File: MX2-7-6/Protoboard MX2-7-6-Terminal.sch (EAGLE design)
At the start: 293 parts

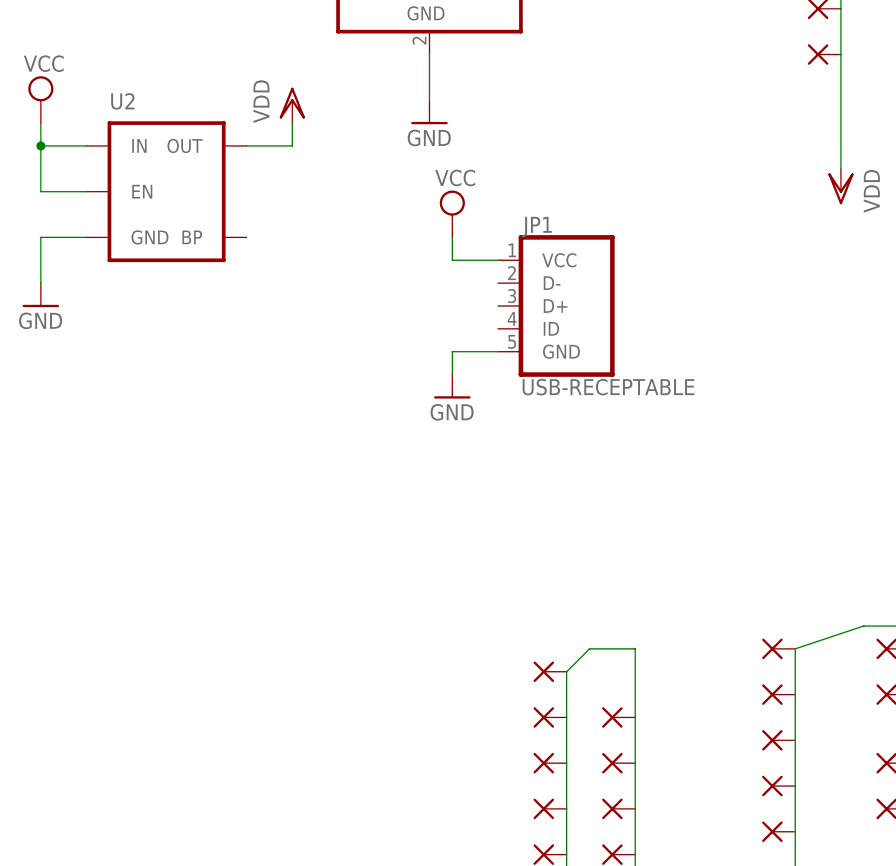
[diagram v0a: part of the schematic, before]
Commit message: Change usb connector
Change to correct usb connecter and moved esp8266 bit more onto the
board.
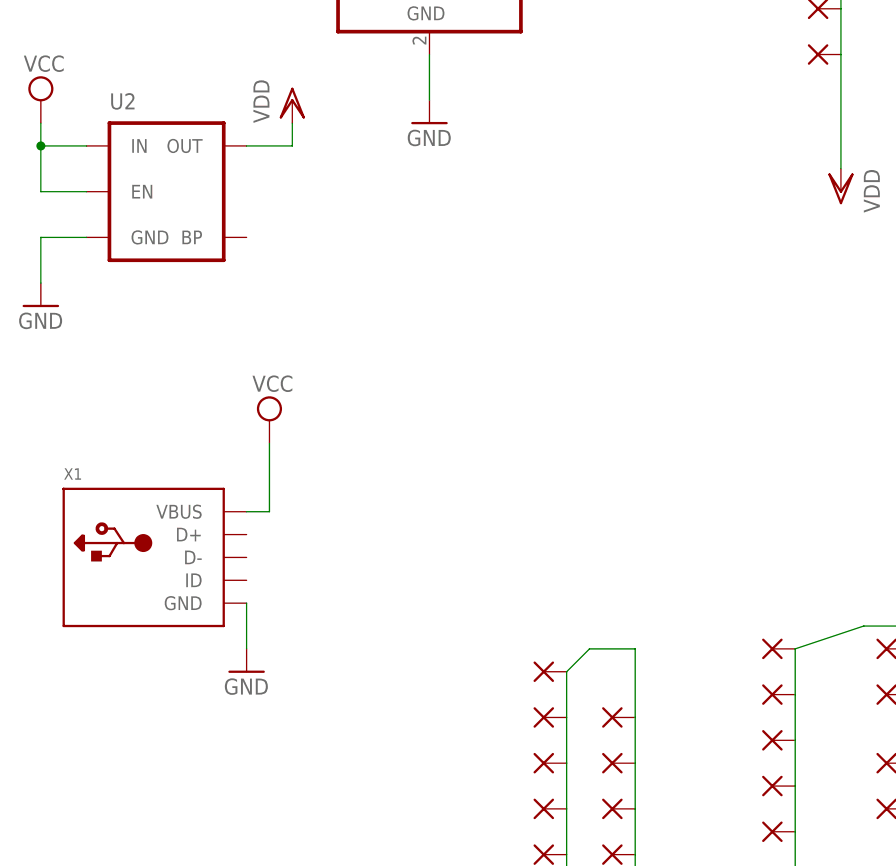
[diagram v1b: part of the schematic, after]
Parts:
- removed JP1: USB-RECEPTABLE, daspilker:USB-RECEPTABLE
- added X1: (no value), microbuilder:USBMICRO_20329
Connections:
- net GND: now also X1.GND; no longer JP1.GND
- net VCC: now also X1.VBUS; no longer JP1.VCC
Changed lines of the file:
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@@
 <part name="PAD38" library="wirepad" deviceset="1,6/0,8" device=""/>
 <part name="GND1" library="supply1" deviceset="GND" device=""/>
-<part name="JP1" library="daspilker" deviceset="USB-RECEPTABLE" device=""/>
-<part name="SUPPLY1" library="supply2" deviceset="VCC" device=""/>
-<part name="GND3" library="supply1" deviceset="GND" device=""/>
 <part name="SUPPLY2" library="supply2" deviceset="VCC" device=""/>
 <part name="GND5" library="supply1" deviceset="GND" device=""/>
@@
 <part name="JP7" library="adafruit" deviceset="PINHD-1X1" device="CB"/>
 <part name="JP8" library="adafruit" deviceset="PINHD-1X1" device="CB"/>
+<part name="X1" library="microbuilder" deviceset="USB" device="MICRO_20329"/>
+<part name="SUPPLY3" library="supply2" deviceset="VCC" device=""/>
+<part name="GND6" library="supply1" deviceset="GND" device=""/>
 </parts>
 <sheets>
@@
 </instance>
 <instance part="GND1" gate="1" x="38.1" y="40.64"/>
-<instance part="JP1" gate="G$1" x="-12.7" y="27.94"/>
-<instance part="SUPPLY1" gate="G$1" x="-25.4" y="38.1"/>
-<instance part="GND3" gate="1" x="-25.4" y="17.78"/>
 <instance part="SUPPLY2" gate="G$1" x="-71.12" y="50.8"/>
 <instance part="GND5" gate="1" x="-71.12" y="27.94"/>
@@
 <instance part="JP7" gate="G$1" x="170.18" y="-35.56" rot="R180"/>
 <instance part="JP8" gate="G$1" x="170.18" y="-40.64" rot="R180"/>
+<instance part="X1" gate="G$1" x="-58.42" y="0"/>
+<instance part="SUPPLY3" gate="G$1" x="-45.72" y="15.24"/>
+<instance part="GND6" gate="1" x="-48.26" y="-12.7"/>
 </instances>
 <busses>
@@
 </segment>
 <segment>
-<pinref part="JP1" gate="G$1" pin="GND"/>
-<pinref part="GND3" gate="1" pin="GND"/>
-<wire x1="-20.32" y1="22.86" x2="-25.4" y2="22.86" width="0.1524" layer="91"/>
-<wire x1="-25.4" y1="22.86" x2="-25.4" y2="20.32" width="0.1524" layer="91"/>
-</segment>
-<segment>
 <pinref part="GND5" gate="1" pin="GND"/>
 <wire x1="-71.12" y1="30.48" x2="-71.12" y2="35.56" width="0.1524" layer="91"/>
@@
 <wire x1="-71.12" y1="35.56" x2="-66.04" y2="35.56" width="0.1524" layer="91"/>
 </segment>
+<segment>
+<pinref part="X1" gate="G$1" pin="GND"/>
+<pinref part="GND6" gate="1" pin="GND"/>
+<wire x1="-48.26" y1="-5.08" x2="-48.26" y2="-10.16" width="0.1524" layer="91"/>
+</segment>
 </net>
 <net name="VCC" class="0">
@@
 <pinref part="DC" gate="G$1" pin="VIN"/>
 <wire x1="-45.72" y1="63.5" x2="-40.64" y2="63.5" width="0.1524" layer="91"/>
-</segment>
-<segment>
-<pinref part="JP1" gate="G$1" pin="VCC"/>
-<pinref part="SUPPLY1" gate="G$1" pin="VCC"/>
-<wire x1="-20.32" y1="33.02" x2="-25.4" y2="33.02" width="0.1524" layer="91"/>
-<wire x1="-25.4" y1="33.02" x2="-25.4" y2="35.56" width="0.1524" layer="91"/>
 </segment>
 <segment>
@@
 <junction x="-71.12" y="45.72"/>
 </segment>
-</net>
+<segment>
+<pinref part="X1" gate="G$1" pin="VBUS"/>
+<pinref part="SUPPLY3" gate="G$1" pin="VCC"/>
+<wire x1="-48.26" y1="5.08" x2="-45.72" y2="5.08" width="0.1524" layer="91"/>
+<wire x1="-45.72" y1="5.08" x2="-45.72" y2="12.7" width="0.1524" layer="91"/>
+</segment>
+</net>

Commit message: Update esp component and usb
test
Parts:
- removed JP4: (no value), adafruit:PINHD-1X1-BIGPOGO
- removed JP6, JP7, JP8: (no value), adafruit:PINHD-1X1CB
- removed PAD1, PAD100, PAD101, PAD102, PAD103, PAD106, PAD107, PAD108, PAD109, PAD110, PAD111, PAD112, PAD115, PAD116, PAD117, PAD118, PAD119, PAD120, PAD121, PAD124, PAD125, PAD126, PAD127, PAD128, PAD129, PAD130, PAD133, PAD134, PAD135, PAD136, PAD137, PAD138, PAD139, PAD142, PAD143, PAD144, PAD145, PAD146, PAD147, PAD148, PAD151, PAD152, PAD153, PAD154, PAD155, PAD156, PAD157, PAD160, PAD161, PAD162, PAD163, PAD164, PAD165, PAD166, PAD169, PAD170, PAD171, PAD172, PAD173, PAD174, PAD175, PAD178, PAD179, PAD180, PAD181, PAD182, PAD183, PAD184, PAD187, PAD188, PAD189, PAD190, PAD191, PAD192, PAD193, PAD196, PAD197, PAD198, PAD199, PAD2, PAD200, PAD201, PAD202, PAD205, PAD206, PAD207, PAD208, PAD209, PAD210, PAD211, PAD214, PAD215, PAD216, PAD217, PAD218, PAD219, PAD220, PAD260, PAD261, PAD262, PAD263, PAD264, PAD265, PAD266, PAD269, PAD270, PAD271, PAD272, PAD273, PAD274, PAD275, PAD278, PAD279, PAD280, PAD281, PAD282, PAD283, PAD284, PAD287, PAD288, PAD289, PAD290, PAD291, PAD292, PAD293, PAD296, PAD297, PAD298, PAD299, PAD300, PAD301, PAD302, PAD305, PAD306, PAD307, PAD308, PAD309, PAD310, PAD311, PAD314, PAD315, PAD316, PAD317, PAD318, PAD319, PAD320, PAD332, PAD333, PAD334, PAD335, PAD336, PAD337, PAD338, PAD341, PAD342, PAD343, PAD344, PAD345, PAD346, PAD347, PAD350, PAD351, PAD352, PAD353, PAD354, PAD355, PAD356, PAD359, PAD360, PAD361, PAD362, PAD363, PAD364, PAD365, PAD368, PAD369, PAD370, PAD371, PAD372, PAD373, PAD374, PAD377, PAD378, PAD379, PAD380, PAD381, PAD382, PAD383, PAD385, PAD386, PAD387, PAD388, PAD389, PAD391, PAD392, PAD393, PAD394, PAD79, PAD80, PAD81, PAD82, PAD83, PAD84, PAD85, PAD88, PAD89, PAD90, PAD91, PAD92, PAD93, PAD94, PAD97, PAD98, PAD99: (no value), wirepad:1,6/0,8
- added J10, J11, J12, J13, J14, J15, J16, J17, J18, J19, J2, J20, J21, J22, J23, J24, J25, J26, J27, J28, J29, J3, J30, J4, J5, J6, J7, J8, J9: (no value), SparkFun-Connectors:M07NO_SILK
- added J31: (no value), SparkFun-Connectors:M05NO_SILK
- added J32: (no value), SparkFun-Connectors:M031X03_NO_SILK
- added J36, J37, J38: (no value), SparkFun-Connectors:M01PTH_NO_SILK_YES_STOP
- added JP1: (no value), adafruit:PINHD-1X1-BIGPOGO
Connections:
- removed net N$40: PAD377.P, PAD378.P, PAD379.P, PAD380.P, PAD381.P, PAD382.P, PAD383.P
- removed net N$41: PAD385.P, PAD386.P, PAD387.P, PAD388.P, PAD389.P
- new net N$6: J4.1, J4.2, J4.3, J4.4, J4.5, J4.6, J4.7
- net N$1: now also J2.1, J2.2, J2.3, J2.4, J2.5, J2.6, J2.7; no longer PAD391.P, PAD392.P, PAD393.P, PAD394.P
- net N$10: now also J8.1, J8.2, J8.3, J8.4, J8.5, J8.6, J8.7; no longer PAD106.P, PAD107.P, PAD108.P, PAD109.P, PAD110.P, PAD111.P, PAD112.P
- net N$11: now also J9.1, J9.2, J9.3, J9.4, J9.5, J9.6, J9.7; no longer PAD115.P, PAD116.P, PAD117.P, PAD118.P, PAD119.P, PAD120.P, PAD121.P
- net N$12: now also J10.1, J10.2, J10.3, J10.4, J10.5, J10.6, J10.7; no longer PAD124.P, PAD125.P, PAD126.P, PAD127.P, PAD128.P, PAD129.P, PAD130.P
- net N$13: now also J11.1, J11.2, J11.3, J11.4, J11.5, J11.6, J11.7; no longer PAD133.P, PAD134.P, PAD135.P, PAD136.P, PAD137.P, PAD138.P, PAD139.P
- net N$14: now also J12.1, J12.2, J12.3, J12.4, J12.5, J12.6, J12.7; no longer PAD142.P, PAD143.P, PAD144.P, PAD145.P, PAD146.P, PAD147.P, PAD148.P
- net N$15: now also J13.1, J13.2, J13.3, J13.4, J13.5, J13.6, J13.7; no longer PAD151.P, PAD152.P, PAD153.P, PAD154.P, PAD155.P, PAD156.P, PAD157.P
- net N$16: now also J14.1, J14.2, J14.3, J14.4, J14.5, J14.6, J14.7; no longer PAD160.P, PAD161.P, PAD162.P, PAD163.P, PAD164.P, PAD165.P, PAD166.P
- net N$17: now also J15.1, J15.2, J15.3, J15.4, J15.5, J15.6, J15.7; no longer PAD169.P, PAD170.P, PAD171.P, PAD172.P, PAD173.P, PAD174.P, PAD175.P
- net N$18: now also J16.1, J16.2, J16.3, J16.4, J16.5, J16.6, J16.7; no longer PAD178.P, PAD179.P, PAD180.P, PAD181.P, PAD182.P, PAD183.P, PAD184.P
- net N$19: now also J17.1, J17.2, J17.3, J17.4, J17.5, J17.6, J17.7; no longer PAD187.P, PAD188.P, PAD189.P, PAD190.P, PAD191.P, PAD192.P, PAD193.P
- net N$2: now also J36.1, JP3.1; no longer JP2.1, JP6.1
- net N$20: now also J18.1, J18.2, J18.3, J18.4, J18.5, J18.6, J18.7; no longer PAD196.P, PAD197.P, PAD198.P, PAD199.P, PAD200.P, PAD201.P, PAD202.P
- net N$21: now also J19.1, J19.2, J19.3, J19.4, J19.5, J19.6, J19.7; no longer PAD205.P, PAD206.P, PAD207.P, PAD208.P, PAD209.P, PAD210.P, PAD211.P
- net N$22: now also J20.1, J20.2, J20.3, J20.4, J20.5, J20.6, J20.7; no longer PAD214.P, PAD215.P, PAD216.P, PAD217.P, PAD218.P, PAD219.P, PAD220.P
- net N$27: now also J21.1, J21.2, J21.3, J21.4, J21.5, J21.6, J21.7; no longer PAD260.P, PAD261.P, PAD262.P, PAD263.P, PAD264.P, PAD265.P, PAD266.P
- net N$28: now also J22.1, J22.2, J22.3, J22.4, J22.5, J22.6, J22.7; no longer PAD269.P, PAD270.P, PAD271.P, PAD272.P, PAD273.P, PAD274.P, PAD275.P
- net N$29: now also J23.1, J23.2, J23.3, J23.4, J23.5, J23.6, J23.7; no longer PAD278.P, PAD279.P, PAD280.P, PAD281.P, PAD282.P, PAD283.P, PAD284.P
- net N$3: now also J37.1, JP2.1; no longer PAD1.P, PAD2.P
- net N$30: now also J24.1, J24.2, J24.3, J24.4, J24.5, J24.6, J24.7; no longer PAD287.P, PAD288.P, PAD289.P, PAD290.P, PAD291.P, PAD292.P, PAD293.P
- net N$31: now also J25.1, J25.2, J25.3, J25.4, J25.5, J25.6, J25.7; no longer PAD296.P, PAD297.P, PAD298.P, PAD299.P, PAD300.P, PAD301.P, PAD302.P
- net N$32: now also J26.1, J26.2, J26.3, J26.4, J26.5, J26.6, J26.7; no longer PAD305.P, PAD306.P, PAD307.P, PAD308.P, PAD309.P, PAD310.P, PAD311.P
- net N$33: now also J27.1, J27.2, J27.3, J27.4, J27.5, J27.6, J27.7; no longer PAD314.P, PAD315.P, PAD316.P, PAD317.P, PAD318.P, PAD319.P, PAD320.P
- net N$35: now also J28.1, J28.2, J28.3, J28.4, J28.5, J28.6, J28.7; no longer PAD332.P, PAD333.P, PAD334.P, PAD335.P, PAD336.P, PAD337.P, PAD338.P
- net N$36: now also J29.1, J29.2, J29.3, J29.4, J29.5, J29.6, J29.7; no longer PAD341.P, PAD342.P, PAD343.P, PAD344.P, PAD345.P, PAD346.P, PAD347.P
- net N$37: now also J30.1, J30.2, J30.3, J30.4, J30.5, J30.6, J30.7; no longer PAD350.P, PAD351.P, PAD352.P, PAD353.P, PAD354.P, PAD355.P, PAD356.P
- net N$38: now also J31.1, J31.2, J31.3, J31.4, J31.5; no longer PAD359.P, PAD360.P, PAD361.P, PAD362.P, PAD363.P, PAD364.P, PAD365.P
- net N$39: now also J32.1, J32.2, J32.3; no longer PAD368.P, PAD369.P, PAD370.P, PAD371.P, PAD372.P, PAD373.P, PAD374.P
- net N$4: now also J38.1, JP1.1; no longer JP3.1, JP7.1
- net N$5: now also J3.1, J3.2, J3.3, J3.4, J3.5, J3.6, J3.7; no longer JP4.1, JP8.1
- net N$7: now also J5.1, J5.2, J5.3, J5.4, J5.5, J5.6, J5.7; no longer PAD79.P, PAD80.P, PAD81.P, PAD82.P, PAD83.P, PAD84.P, PAD85.P
- net N$8: now also J6.1, J6.2, J6.3, J6.4, J6.5, J6.6, J6.7; no longer PAD88.P, PAD89.P, PAD90.P, PAD91.P, PAD92.P, PAD93.P, PAD94.P
- net N$9: now also J7.1, J7.2, J7.3, J7.4, J7.5, J7.6, J7.7; no longer PAD100.P, PAD101.P, PAD102.P, PAD103.P, PAD97.P, PAD98.P, PAD99.P
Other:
- moved on the sheet: JP2, JP3, X1
